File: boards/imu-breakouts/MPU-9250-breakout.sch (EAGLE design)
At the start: 5 parts, among them IC1 MPU-9250

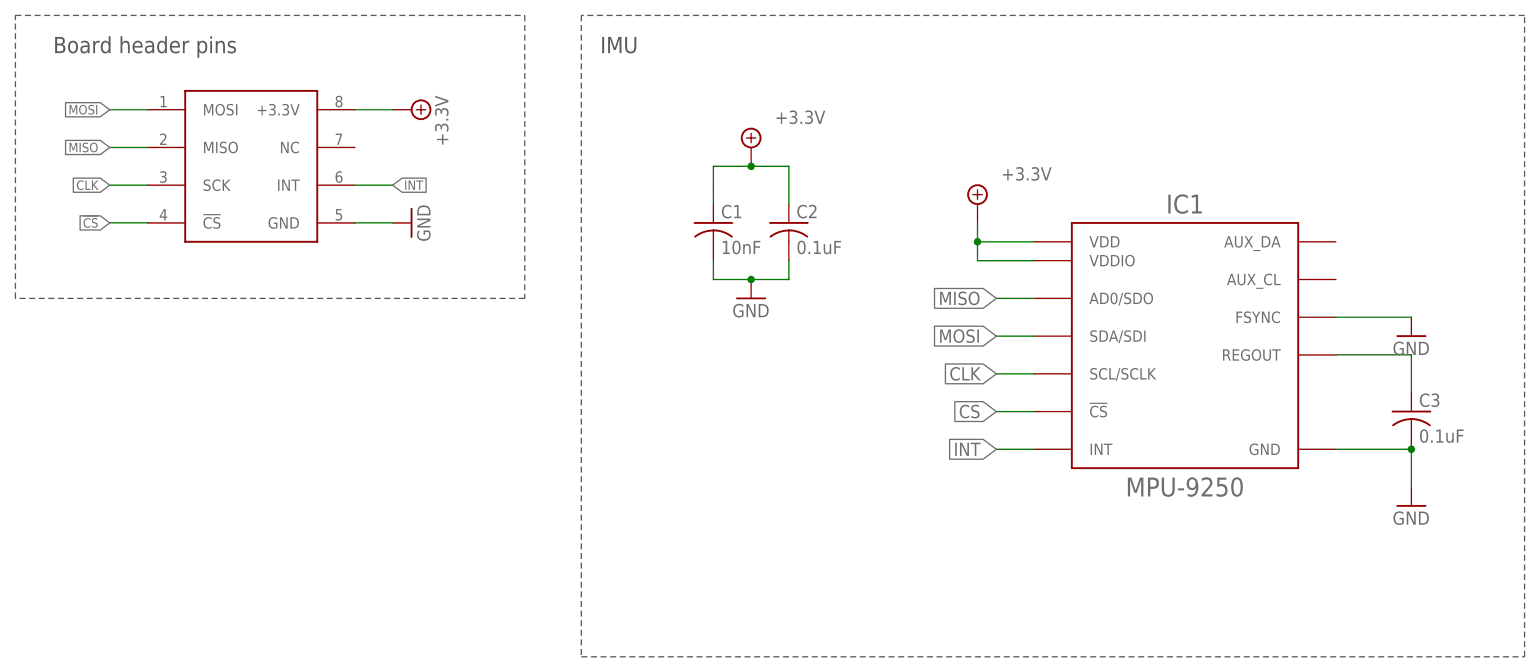
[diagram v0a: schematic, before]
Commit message: Applied same adjustments to MPU 9250
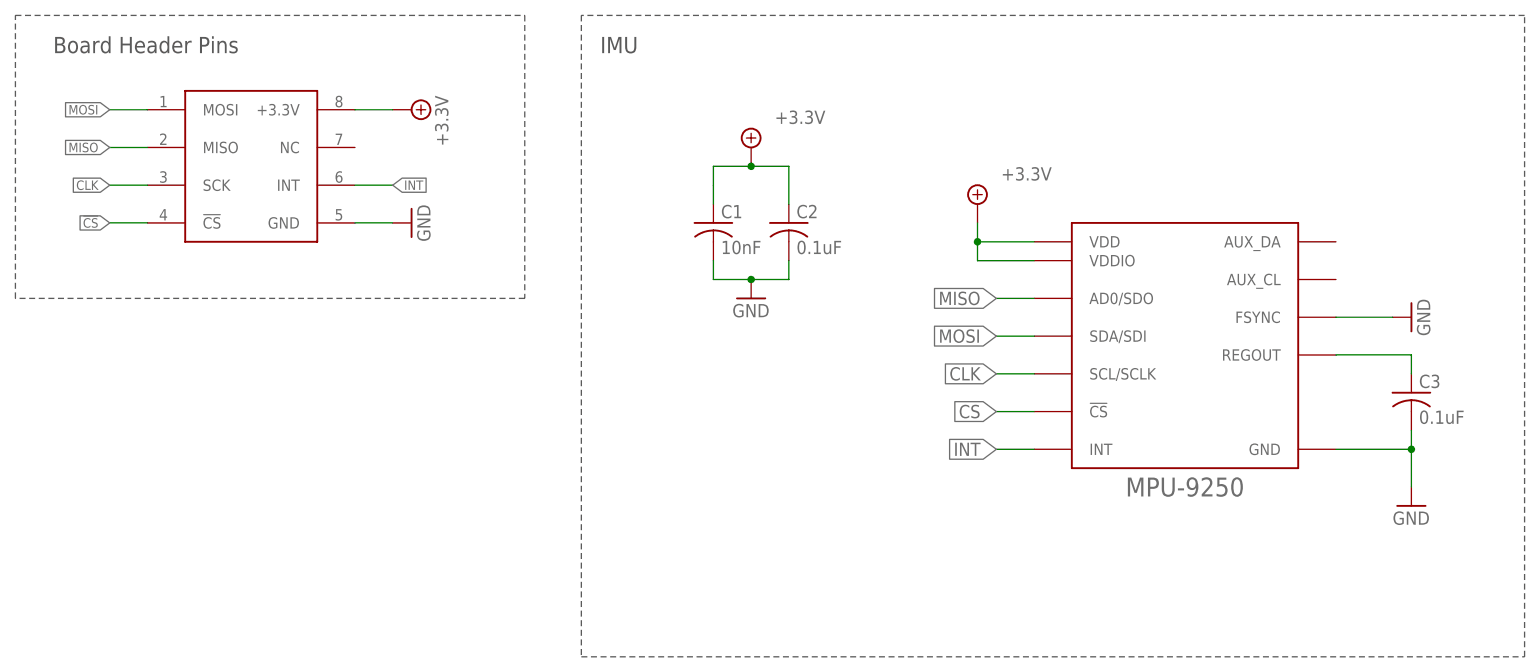
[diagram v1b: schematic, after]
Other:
- note added: "Board Header Pins"
- note removed: "Board header pins"
- moved on the sheet: C3
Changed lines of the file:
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@@
 <?xml version="1.0" encoding="utf-8"?>
 <!DOCTYPE eagle SYSTEM "eagle.dtd">
-<eagle version="9.5.1">
+<eagle version="9.5.2">
 <drawing>
 <settings>
-<setting alwaysvectorfont="no"/>
+<setting alwaysvectorfont="yes"/>
 <setting verticaltext="up"/>
 </settings>
-<grid distance="0.1" unitdist="inch" unit="inch" style="lines" multiple="1" display="no" altdistance="0.01" altunitdist="inch" altunit="inch"/>
+<grid distance="0.1" unitdist="inch" unit="inch" style="lines" multiple="1" display="yes" altdistance="0.01" altunitdist="inch" altunit="inch"/>
 <layers>
 <layer number="1" name="Top" color="4" fill="1" visible="no" active="no"/>
@@
 <parts>
 <part name="FRAME1" library="RoboJackets-Frames" deviceset="FRAME_A_L" device="">
-<attribute name="REVISION" value=""/>
-<attribute name="SCH_DESC" value=""/>
-<attribute name="TEAM" value=""/>
+<attribute name="REVISION" value="1.0"/>
+<attribute name="SCH_DESC" value="Breakout for MPU 9250 IMU"/>
+<attribute name="TEAM" value="RoboCup SSL"/>
 </part>
 <part name="KIT1" library="RoboJackets-Boards" deviceset="IMU" device="IMU-KIT"/>
@@
 <wire x1="218.44" y1="175.26" x2="91.44" y2="175.26" width="0.1524" layer="97" style="shortdash"/>
 <text x="93.98" y="170.18" size="2.1844" layer="97">IMU</text>
-<text x="20.32" y="170.18" size="2.1844" layer="97">Board header pins</text>
+<text x="20.32" y="170.18" size="2.1844" layer="97">Board Header Pins</text>
 <wire x1="91.44" y1="175.26" x2="91.44" y2="88.9" width="0.1524" layer="97" style="shortdash"/>
 <wire x1="91.44" y1="88.9" x2="218.44" y2="88.9" width="0.1524" layer="97" style="shortdash"/>
@@
 </instance>
 <instance part="IC1" gate="G$1" x="172.72" y="132.08" smashed="yes">
-<attribute name="NAME" x="172.72" y="148.59" size="2.54" layer="95" align="bottom-center"/>
 <attribute name="VALUE" x="172.72" y="113.03" size="2.54" layer="96" align="top-center"/>
 </instance>
@@
 <attribute name="VALUE" x="110.236" y="143.129" size="1.778" layer="96"/>
 </instance>
-<instance part="GND7" gate="1" x="203.2" y="132.08" smashed="yes">
-<attribute name="VALUE" x="200.66" y="129.54" size="1.778" layer="96"/>
-</instance>
-<instance part="C3" gate="G$1" x="203.2" y="121.92" smashed="yes">
-<attribute name="NAME" x="204.216" y="122.555" size="1.778" layer="95"/>
-<attribute name="VALUE" x="204.216" y="117.729" size="1.778" layer="96"/>
+<instance part="GND7" gate="1" x="203.2" y="134.62" smashed="yes" rot="R90">
+<attribute name="VALUE" x="205.74" y="132.08" size="1.778" layer="96" rot="R90"/>
+</instance>
+<instance part="C3" gate="G$1" x="203.2" y="124.46" smashed="yes">
+<attribute name="NAME" x="204.216" y="125.095" size="1.778" layer="95"/>
+<attribute name="VALUE" x="204.216" y="120.269" size="1.778" layer="96"/>
 </instance>
 <instance part="GND8" gate="1" x="203.2" y="109.22" smashed="yes">
@@
 <pinref part="IC1" gate="G$1" pin="FSYNC"/>
 <pinref part="GND7" gate="1" pin="GND"/>
-<wire x1="193.04" y1="134.62" x2="203.2" y2="134.62" width="0.1524" layer="91"/>
+<wire x1="193.04" y1="134.62" x2="200.66" y2="134.62" width="0.1524" layer="91"/>
 </segment>
 <segment>
 <pinref part="C3" gate="G$1" pin="2"/>
 <pinref part="GND8" gate="1" pin="GND"/>
+<wire x1="203.2" y1="119.38" x2="203.2" y2="116.84" width="0.1524" layer="91"/>
+<pinref part="IC1" gate="G$1" pin="GND"/>
 <wire x1="203.2" y1="116.84" x2="203.2" y2="111.76" width="0.1524" layer="91"/>
-<pinref part="IC1" gate="G$1" pin="GND"/>
-<wire x1="193.04" y1="116.84" x2="203.2" y2="116.84" width="0.1524" layer="91"/>
 <junction x="203.2" y="116.84"/>
+<wire x1="203.2" y1="116.84" x2="193.04" y2="116.84" width="0.1524" layer="91"/>
 </segment>
 <segment>
@@
 <wire x1="193.04" y1="129.54" x2="203.2" y2="129.54" width="0.1524" layer="91"/>
 <pinref part="C3" gate="G$1" pin="1"/>
-<wire x1="203.2" y1="129.54" x2="203.2" y2="124.46" width="0.1524" layer="91"/>
-</segment>
-</net>
+<wire x1="203.2" y1="129.54" x2="203.2" y2="127" width="0.1524" layer="91"/>
+</segment>
+</net>

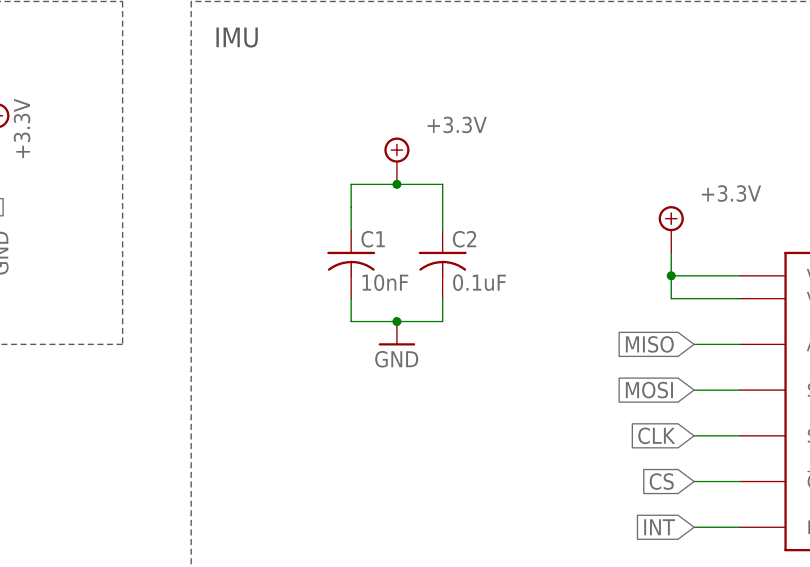
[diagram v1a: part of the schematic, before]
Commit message: Fixed board and text for ICM 42605
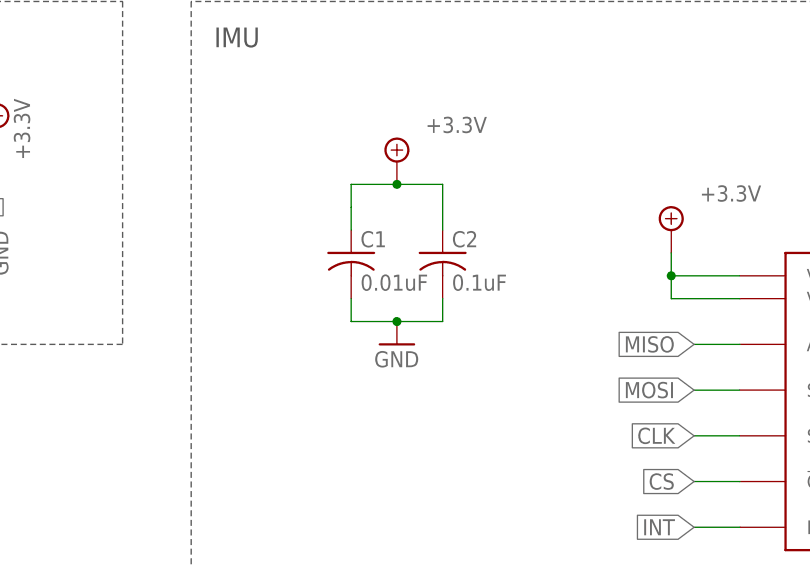
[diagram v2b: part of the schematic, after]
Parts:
- C1: value 10nF -> 0.01uF
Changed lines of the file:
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@@
 <part name="C2" library="rcl" library_urn="urn:adsk.eagle:library:334" deviceset="C-US" device="C0603" package3d_urn="urn:adsk.eagle:package:23616/2" value="0.1uF"/>
 <part name="GND6" library="supply1" library_urn="urn:adsk.eagle:library:371" deviceset="GND" device=""/>
-<part name="C1" library="rcl" library_urn="urn:adsk.eagle:library:334" deviceset="C-US" device="C0603" package3d_urn="urn:adsk.eagle:package:23616/2" value="10nF"/>
+<part name="C1" library="rcl" library_urn="urn:adsk.eagle:library:334" deviceset="C-US" device="C0603" package3d_urn="urn:adsk.eagle:package:23616/2" value="0.01uF"/>
 <part name="GND7" library="supply1" library_urn="urn:adsk.eagle:library:371" deviceset="GND" device=""/>
 <part name="C3" library="rcl" library_urn="urn:adsk.eagle:library:334" deviceset="C-US" device="C0603" package3d_urn="urn:adsk.eagle:package:23616/2" value="0.1uF"/>
